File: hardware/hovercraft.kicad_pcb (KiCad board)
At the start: 2 copper layers, 9 parts, among them J1 USB_OTG, U1 ATMEGA32U2-AU, Y1 Crystal_GND24

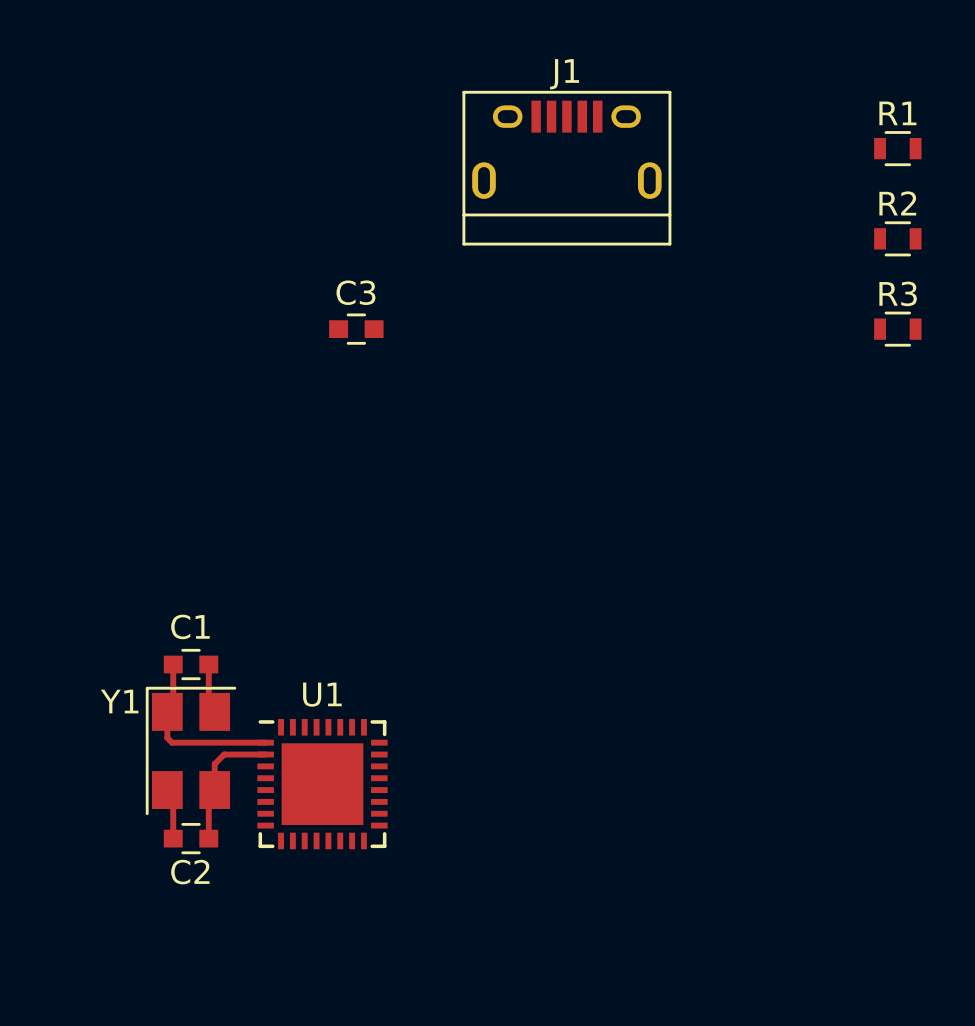
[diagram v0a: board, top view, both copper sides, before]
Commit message: Finish the basic layout of the micro. Next the power needs to be sorted and how the micro will talk to the motors
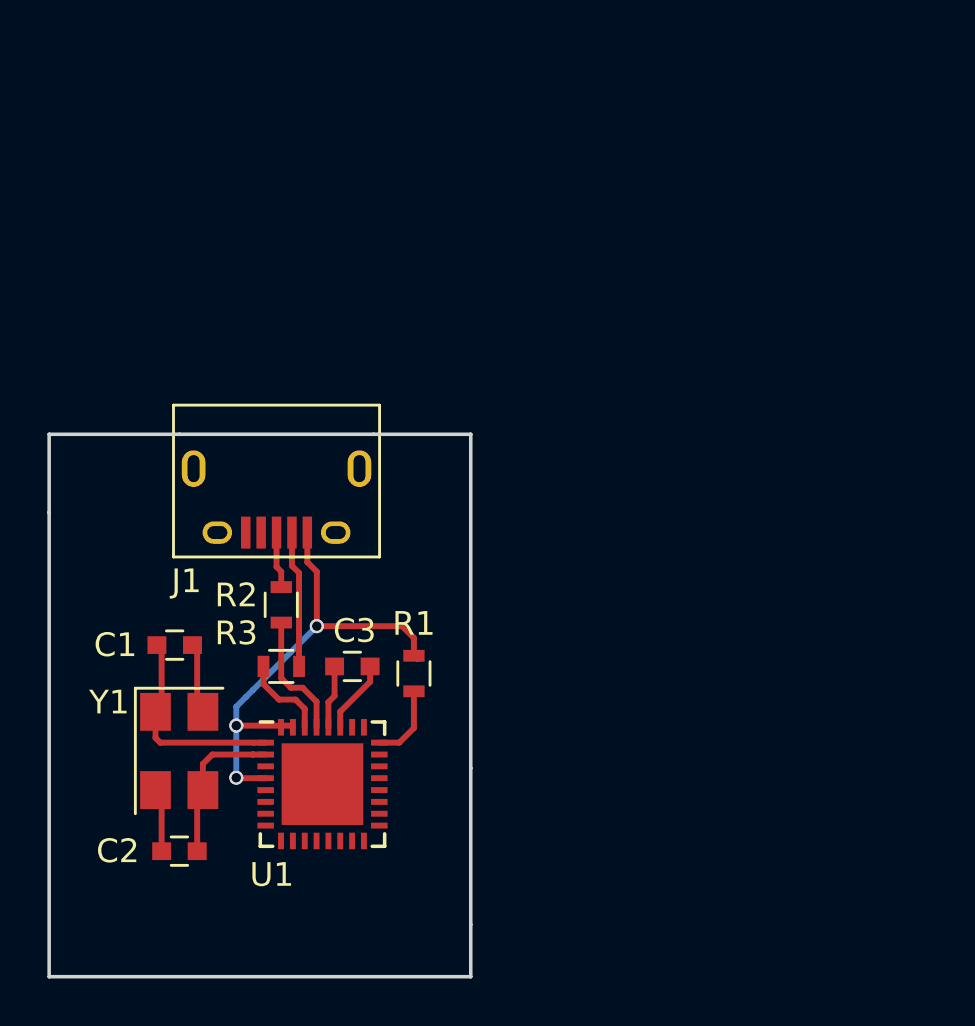
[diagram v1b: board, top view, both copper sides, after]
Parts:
- moved R2 30.3 mm to (135.3, 109.4), turned to 90 degrees
- moved R1 30.1 mm to (140.9, 112.3), turned to 90 degrees
- moved R3 29.7 mm to (135.3, 112.0)
- moved J1 19.3 mm to (135.1, 105.0), turned to 180 degrees
- moved C3 14.2 mm to (138.3, 112.0)
- moved C1 1.07 mm to (130.8, 111.1)
- moved C2 0.72 mm to (131.0, 119.8)
- moved Y1 0.50 mm to (130.9, 115.6)
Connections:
- U1 pad 33: (no net) -> GND
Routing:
- net VCC: track 0.00 -> 20.9 mm, vias 0 -> 3
- net /USB_N: track 0.00 -> 5.77 mm
- net Net-(R2-Pad1): track 0.00 -> 5.33 mm
- net GND: track 4.26 -> 9.19 mm
- net Net-(R3-Pad1): track 0.00 -> 3.70 mm
- net Net-(R1-Pad1): track 0.00 -> 3.27 mm
- net Net-(C3-Pad2): track 0.00 -> 3.09 mm
- net /USB_P: track 0.00 -> 2.38 mm
- net Net-(C1-Pad2): track 7.44 -> 9.31 mm
- net Net-(C2-Pad2): track 5.57 -> 6.99 mm
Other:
- board outline added: 17.8 x 22.9 mm
- net class Default: clearance 0.2 -> 0.15
- rule trace_clearance: 0.2 -> 0.15

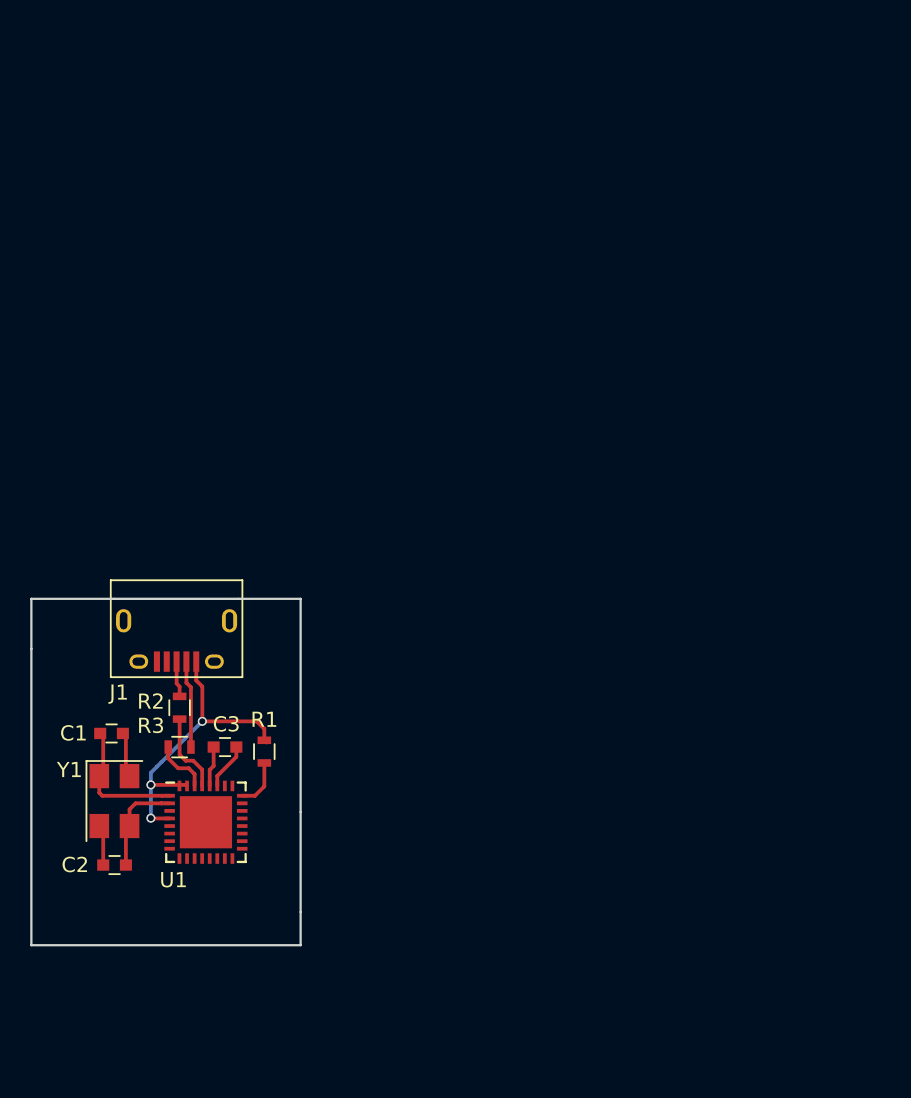
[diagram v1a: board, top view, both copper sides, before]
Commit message: Filled out the schematic with servo and power connectors and populated these on the PCB
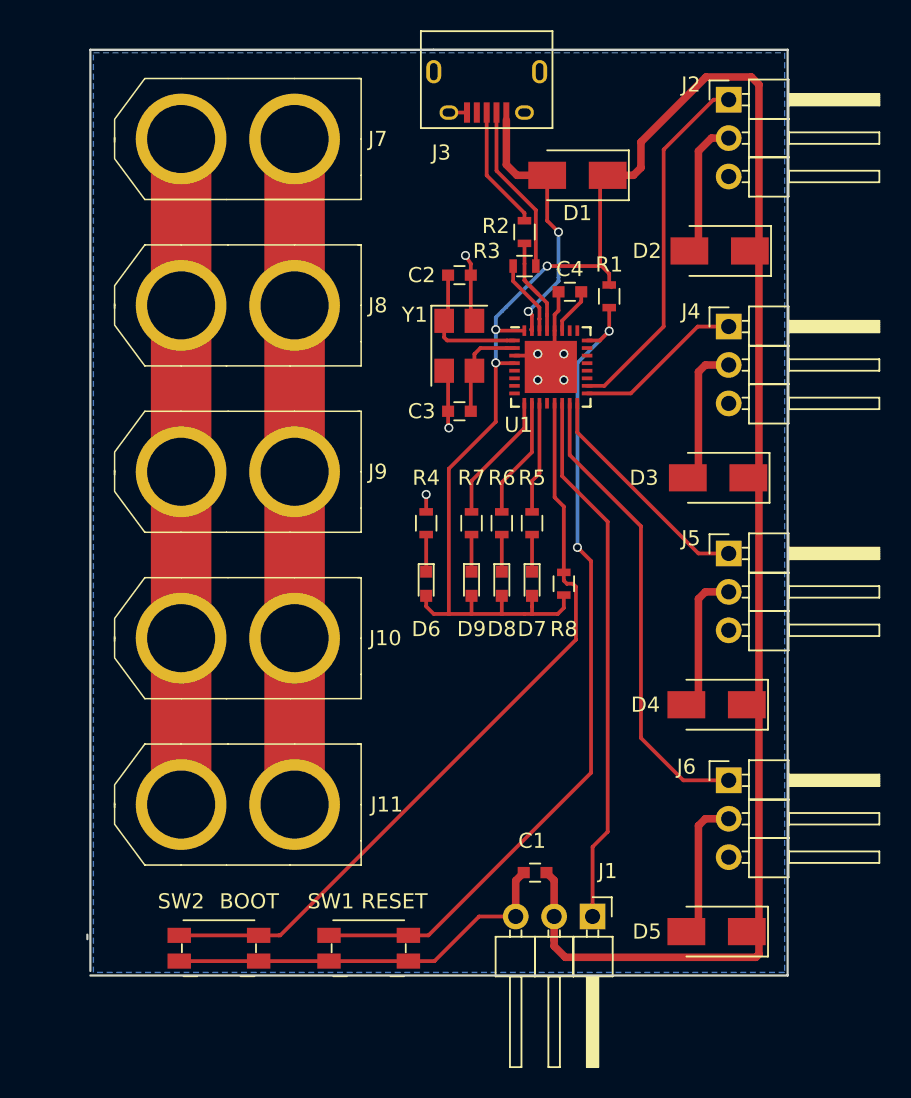
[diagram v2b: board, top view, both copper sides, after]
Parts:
- added C4: 1uF, Capacitors_SMD:C_0603, F.Cu at (161.1, 81.9)
- added D1: D_Schottky_Small, Diodes_SMD:D_SMA, F.Cu at (161.6, 74.2)
- added D2: D_Schottky_Small, Diodes_SMD:D_SMA, F.Cu at (171.0, 79.2)
- added D3: D_Schottky_Small, Diodes_SMD:D_SMA, F.Cu at (170.9, 94.2)
- added D4: D_Schottky_Small, Diodes_SMD:D_SMA, F.Cu at (170.8, 109.2)
- added D5: D_Schottky_Small, Diodes_SMD:D_SMA, F.Cu at (170.8, 124.2)
- added D6: POWER, LEDs:LED_0603, F.Cu at (151.6, 101.2)
- added D7: GREEN, LEDs:LED_0603, F.Cu at (158.6, 101.2)
- added D8: YELLOW, LEDs:LED_0603, F.Cu at (156.6, 101.2)
- added D9: RED, LEDs:LED_0603, F.Cu at (154.6, 101.2)
- added J10: CONN_01X02, modules:XT60, F.Cu at (135.4, 104.8)
- added J11: CONN_01X02, modules:XT60, F.Cu at (135.4, 115.8)
- added J2: CONN_01X03, Pin_Headers:Pin_Header_Angled_1x03_Pitch2.54mm, F.Cu at (171.6, 69.2)
- added J3: USB_OTG, Connectors:USB_Micro-B, F.Cu at (155.6, 68.7)
- added J4: CONN_01X03, Pin_Headers:Pin_Header_Angled_1x03_Pitch2.54mm, F.Cu at (171.6, 84.2)
- added J5: CONN_01X03, Pin_Headers:Pin_Header_Angled_1x03_Pitch2.54mm, F.Cu at (171.6, 99.2)
- added J6: CONN_01X03, Pin_Headers:Pin_Header_Angled_1x03_Pitch2.54mm, F.Cu at (171.6, 114.2)
- added J7: CONN_01X02, modules:XT60, F.Cu at (135.4, 71.8)
- added J8: CONN_01X02, modules:XT60, F.Cu at (135.4, 82.8)
- added J9: CONN_01X02, modules:XT60, F.Cu at (135.4, 93.8)
- added R4: 1K8, Resistors_SMD:R_0603, F.Cu at (151.6, 97.2)
- added R5: 1K8, Resistors_SMD:R_0603, F.Cu at (158.6, 97.2)
- added R6: 3K, Resistors_SMD:R_0603, F.Cu at (156.6, 97.2)
- added R7: 3K, Resistors_SMD:R_0603, F.Cu at (154.6, 97.2)
- added R8: 10k, Resistors_SMD:R_0603, F.Cu at (160.7, 101.2)
- added SW1: RESET, Buttons_Switches_SMD:Panasonic_EVQPUJ_EVQPUA, F.Cu at (147.8, 125.3)
- added SW2: BOOT, Buttons_Switches_SMD:Panasonic_EVQPUJ_EVQPUA, F.Cu at (137.9, 125.3)
- C1: value 30pF -> 1uF
- C3: value 1uF -> 30pF
- J1: value USB_OTG -> CONN_01X03; footprint Connectors:USB_Micro-B -> Pin_Headers:Pin_Header_Angled_1x03_Pitch2.54mm
- moved C2 45.2 mm to (153.8, 80.8), turned to 180 degrees
- moved R3 39.1 mm to (158.1, 80.2)
- moved R2 38.8 mm to (158.1, 78.0)
- moved U1 37.8 mm to (159.8, 86.9)
- moved Y1 37.8 mm to (153.8, 85.5)
- moved R1 37.8 mm to (163.7, 82.2), turned to 270 degrees
- moved J1 33.0 mm to (162.6, 123.2), turned to 270 degrees
- moved C1 29.5 mm to (158.8, 120.3)
- moved C3 27.1 mm to (153.8, 89.8)
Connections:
- C1 pad 1: GND -> VCC
- C1 pad 2: Net-(C1-Pad2) -> GND
- J1 pad 1: VCC -> /CH4
- J1 pad 2: /USB_N -> VCC
- J1 pad 3: /USB_P -> GND
- R1 pad 1: Net-(R1-Pad1) -> VCC
- R1 pad 2: VCC -> Net-(R1-Pad2)
- U1 pad 1: Net-(C1-Pad2) -> Net-(C2-Pad2)
- U1 pad 14: Net-(U1-Pad14) -> /CH4
- U1 pad 15: Net-(U1-Pad15) -> /CH3
- U1 pad 16: Net-(U1-Pad16) -> /CH2
- U1 pad 17: Net-(U1-Pad17) -> /CH1
- U1 pad 18: Net-(U1-Pad18) -> /CH0
- U1 pad 2: Net-(C2-Pad2) -> Net-(C3-Pad2)
- U1 pad 24: Net-(R1-Pad1) -> Net-(R1-Pad2)
- U1 pad 27: Net-(C3-Pad2) -> Net-(C4-Pad2)
- U1 pad 31: VCC -> /VBUS
- Y1 pad 1: Net-(C1-Pad2) -> Net-(C2-Pad2)
- Y1 pad 3: Net-(C2-Pad2) -> Net-(C3-Pad2)
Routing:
- net VCC: track 20.9 -> 146.1 mm
- net Net-(J10-Pad2): track 0.00 -> 77.0 mm
- net Net-(J10-Pad1): track 0.00 -> 77.0 mm
- net Net-(R1-Pad2): track 0.00 -> 55.5 mm, vias 0 -> 2
- net Net-(R8-Pad1): track 0.00 -> 50.8 mm
- net /CH4: track 0.00 -> 35.6 mm
- net GND: track 9.19 -> 44.1 mm, vias 0 -> 7
- net /CH3: track 0.00 -> 31.0 mm
- net /CH0: track 0.00 -> 24.1 mm
- net /VBUS: track 0.00 -> 18.5 mm, vias 0 -> 2
- net /CH2: track 0.00 -> 15.2 mm
- net /CH1: track 0.00 -> 11.2 mm
- net Net-(C1-Pad2): track 9.31 -> 0.00 mm
- net Net-(D5-Pad2): track 0.00 -> 9.19 mm
- net Net-(D4-Pad2): track 0.00 -> 9.19 mm
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- added copper zone on B.Cu, net GND
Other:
- board size 17.8 x 22.9 mm -> 46.3 x 61.2 mm
- net class Power added: clearance 0.15, trace_width 1, via_dia 1.5, via_drill 1
- board text added: "BOOT"
- board text added: "RESET"

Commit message: Add the HC-12 foot print and repopulate the board to fit it in.
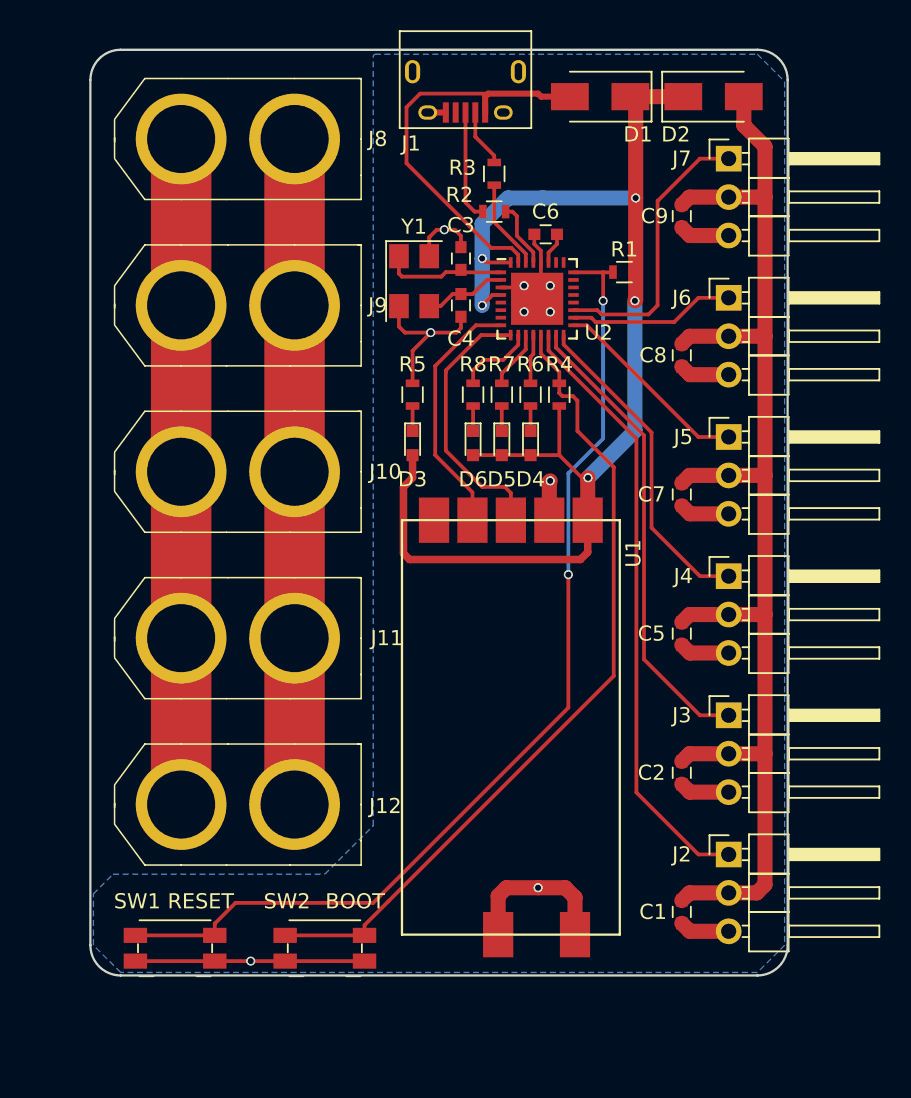
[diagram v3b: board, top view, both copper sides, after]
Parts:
- removed D7: GREEN, LEDs:LED_0603
- removed D8: YELLOW, LEDs:LED_0603
- removed D9: RED, LEDs:LED_0603
- added C5: 1uF, Capacitors_SMD:C_0603, F.Cu at (168.5, 104.5)
- added C6: 1uF, Capacitors_SMD:C_0603, F.Cu at (159.5, 78.1)
- added C7: 1uF, Capacitors_SMD:C_0603, F.Cu at (168.5, 95.3)
- added C8: 1uF, Capacitors_SMD:C_0603, F.Cu at (168.5, 86.1)
- added C9: 1uF, Capacitors_SMD:C_0603, F.Cu at (168.5, 76.9)
- added J12: CONN_01X02, modules:XT60, F.Cu at (135.4, 115.8)
- added U2: ATMEGA32U2-AU, Housings_DFN_QFN:QFN-32-1EP_5x5mm_Pitch0.5mm, F.Cu at (158.9, 82.4)
- C2: value 30pF -> 1uF
- C4: value 1uF -> 30pF
- D3: value D_Schottky_Small -> POWER; footprint Diodes_SMD:D_SMA -> LEDs:LED_0603
- D4: value D_Schottky_Small -> GREEN; footprint Diodes_SMD:D_SMA -> LEDs:LED_0603
- D5: value D_Schottky_Small -> YELLOW; footprint Diodes_SMD:D_SMA -> LEDs:LED_0603
- D6: value POWER -> RED
- J1: value CONN_01X03 -> USB_OTG; footprint Pin_Headers:Pin_Header_Angled_1x03_Pitch2.54mm -> Connectors:USB_Micro-B
- J3: value USB_OTG -> CONN_01X03; footprint Connectors:USB_Micro-B -> Pin_Headers:Pin_Header_Angled_1x03_Pitch2.54mm
- J7: value CONN_01X02 -> CONN_01X03; footprint modules:XT60 -> Pin_Headers:Pin_Header_Angled_1x03_Pitch2.54mm
- R4: value 1K8 -> 10k
- R6: value 3K -> 1K8
- R8: value 10k -> 3K
- U1: value ATMEGA32U2-AU -> HC-12; footprint Housings_DFN_QFN:QFN-32-1EP_5x5mm_Pitch0.5mm -> modules:HC-12
- moved J1 55.1 mm to (154.2, 68.7), turned to 180 degrees
- moved J2 49.9 mm to (171.6, 119.1)
- moved J3 44.2 mm to (171.6, 109.9), turned to 0 degrees
- moved J7 36.2 mm to (171.6, 73.1)
- moved C2 36.0 mm to (168.5, 113.7), turned to 270 degrees
- moved D5 35.3 mm to (156.6, 91.9), turned to 270 degrees
- moved J6 31.9 mm to (171.6, 82.3)
- moved D4 21.2 mm to (158.5, 91.9), turned to 270 degrees
- moved D3 20.3 mm to (150.7, 91.9), turned to 270 degrees
- moved J4 16.5 mm to (171.6, 100.7)
- moved R8 13.9 mm to (154.7, 88.7), turned to 90 degrees
- moved SW1 12.8 mm to (135.0, 125.3)
- moved R4 12.2 mm to (160.4, 88.7), turned to 270 degrees
- moved R5 11.6 mm to (150.7, 88.7)
- moved U1 11.1 mm to (164.4, 97.0), turned to 270 degrees
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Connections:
- C1 pad 1: VCC -> Net-(C1-Pad1)
- C2 pad 1: GND -> Net-(C1-Pad1)
- C2 pad 2: Net-(C2-Pad2) -> GND
- D2 pad 2: Net-(D2-Pad2) -> Net-(C1-Pad1)
- D3 pad 1: VCC -> Net-(D3-Pad1)
- D3 pad 2: Net-(D3-Pad2) -> VCC
- D4 pad 1: VCC -> Net-(D4-Pad1)
- D4 pad 2: Net-(D4-Pad2) -> VCC
- D5 pad 1: VCC -> Net-(D5-Pad1)
- D5 pad 2: Net-(D5-Pad2) -> VCC
- J1 pad 1: /CH4 -> /VBUS
- J1 pad 2: VCC -> /USB_N
- J1 pad 3: GND -> /USB_P
- J2 pad 2: Net-(D2-Pad2) -> Net-(C1-Pad1)
- J3 pad 1: /VBUS -> /CH1
- J3 pad 2: /USB_N -> Net-(C1-Pad1)
- J3 pad 3: /USB_P -> GND
- J4 pad 1: /CH1 -> /CH2
- J4 pad 2: Net-(D3-Pad2) -> Net-(C1-Pad1)
- J5 pad 1: /CH2 -> /CH3
- J5 pad 2: Net-(D4-Pad2) -> Net-(C1-Pad1)
- J6 pad 1: /CH3 -> /CH4
- J6 pad 2: Net-(D5-Pad2) -> Net-(C1-Pad1)
- J7 pad 1: Net-(J10-Pad1) -> /CH5
- J7 pad 2: Net-(J10-Pad2) -> Net-(C1-Pad1)
- R4 pad 1: Net-(D6-Pad1) -> Net-(R4-Pad1)
- R4 pad 2: GND -> VCC
- R5 pad 1: Net-(D7-Pad1) -> Net-(D3-Pad1)
- R5 pad 2: Net-(R5-Pad2) -> GND
- R6 pad 1: Net-(D8-Pad1) -> Net-(D4-Pad1)
- R7 pad 1: Net-(D9-Pad1) -> Net-(D5-Pad1)
- R8 pad 1: Net-(R8-Pad1) -> Net-(D6-Pad1)
- R8 pad 2: VCC -> Net-(R8-Pad2)
- SW2 pad 2: Net-(R8-Pad1) -> Net-(R4-Pad1)
- U1 pad 1: Net-(C2-Pad2) -> VCC
- U1 pad 2: Net-(C3-Pad2) -> GND
- U1 pad 3: GND -> /MCU_TXD
- U1 pad 4: VCC -> /MCU_RXD
- U1 pad 5: Net-(U1-Pad5) -> (no net)
- U1 pad 7: Net-(U1-Pad7) -> GND
- U1 pad 8: Net-(U1-Pad8) -> GND
- Y1 pad 1: Net-(C2-Pad2) -> Net-(C3-Pad2)
- Y1 pad 3: Net-(C3-Pad2) -> Net-(C4-Pad2)
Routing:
- net Net-(C1-Pad1): track 0.00 -> 87.2 mm
- net VCC: track 146.1 -> 85.6 mm, vias 3 -> 5
- net Net-(R4-Pad1): track 0.00 -> 54.8 mm
- net Net-(R8-Pad1): track 50.8 -> 0.00 mm
- net GND: track 44.1 -> 69.8 mm, vias 7 -> 9
- net /CH4: track 35.6 -> 11.0 mm
- net /CH1: track 11.2 -> 31.0 mm
- net /CH5: track 0.00 -> 18.7 mm
- net /MCU_TXD: track 0.00 -> 17.8 mm
- net /CH3: track 31.0 -> 13.3 mm
- net /MCU_RXD: track 0.00 -> 16.7 mm
- net /CH0: track 24.1 -> 40.4 mm
- net Net-(R1-Pad2): track 55.5 -> 67.7 mm
- net Net-(C2-Pad2): track 9.31 -> 0.00 mm
- net Net-(D5-Pad2): track 9.19 -> 0.00 mm
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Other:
- board size 46.3 x 61.2 mm -> 46.1 x 61.2 mm
